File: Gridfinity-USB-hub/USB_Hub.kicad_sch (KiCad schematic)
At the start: 10 parts, among them U1 CH334F, Y1 12MHz

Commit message: V2 complete, ready for review and polish
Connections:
- net at Y1.1: now also U1.3 (XO); no longer U1.4 (XI)
- net at Y1.3: now also U1.4 (XI); no longer U1.3 (XO)

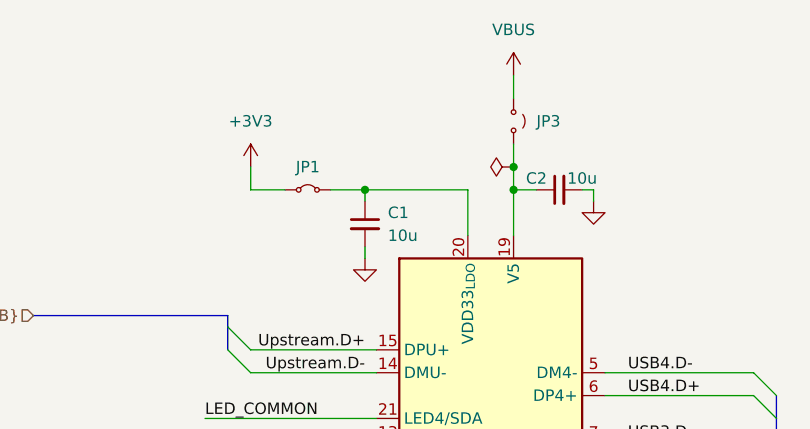
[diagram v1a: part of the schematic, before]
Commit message: Add 3x channels of spare LEDs for general breadboard use, add silkscreen.  Ordered this version
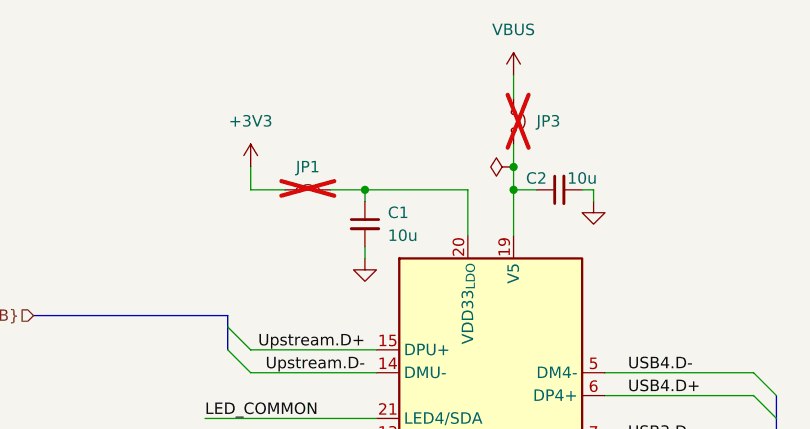
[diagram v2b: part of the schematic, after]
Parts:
- JP1, JP3: now not fitted
- U1: FT Rotation Offset (none) -> 180; JLCPCB Part No. (none) -> C5187527
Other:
- company: (none) -> SK Electronics Consulting LLC
- title: (none) -> USB 2.0 Hub for Gridifinity
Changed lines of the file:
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@@
 	(generator_version "9.0")
 	(paper "A4")
+	(title_block
+		(title "USB 2.0 Hub for Gridifinity")
+		(date "2026-02-16")
+		(rev "2")
+		(company "SK Electronics Consulting LLC")
+	)
 	(bus_alias "LED"
 		(members "A" "K")
@@
 		(in_bom yes)
 		(on_board yes)
-		(dnp no)
+		(dnp yes)
 		(property "Reference" "JP1"
 			(at 101.6 48.26 0)
@@
 			)
 		)
+		(property "JLCPCB Part No." "C5187527"
+			(at 121.92 83.82 0)
+			(effects
+				(font
+					(size 1.27 1.27)
+				)
+				(hide yes)
+			)
+		)
+		(property "FT Rotation Offset" "180"
+			(at 121.92 83.82 0)
+			(effects
+				(font
+					(size 1.27 1.27)
+				)
+				(hide yes)
+			)
+		)
 		(pin "6"
 		)
@@
 		(in_bom yes)
 		(on_board yes)
-		(dnp no)
+		(dnp yes)
 		(fields_autoplaced yes)
 		(property "Reference" "JP3"
